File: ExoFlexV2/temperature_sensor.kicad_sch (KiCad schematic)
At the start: 32 parts, among them U31 SN74LVC3G14DCUT_V2, U33 SN74HC7032D_V2, U42 ADCMP602BRMZ, U43 ADCMP602BRMZ, U44 ADCMP602BRMZ, U6 SN74HC7032D_V2, U8 SN74LV4T08PWR_V2

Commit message: quque truc
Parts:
- removed R52, R53, R54: R_Small_US, Resistor_SMD:R_0603_1608Metric, symbol Device:R_Small_US
- removed RV2, RV3, RV4: *, symbol Device:R_Potentiometer_US
- removed TP30, TP31, TP32: 5005, FootPrint:KEYSTONE_5005, symbol SymLib:5005
- added C123, C124, C125, C126, C127, C128: 1nF, Capacitor_SMD:C_0603_1608Metric, symbol Device:C
- added R100, R104, R105, R106, R107, R108, R109, R98, R99: 0 ohm, Resistor_SMD:R_0603_1608Metric, symbol Device:R_Small_US
- added R101, R102, R103, R110, R111, R112: 7,5k, Resistor_SMD:R_0603_1608Metric, symbol Device:R_Small_US
- added TP73, TP74, TP75, TP76, TP77, TP78, TP82: 5005, FootPrint:KEYSTONE_5005, symbol SymLib:5005
- renumbered C98 to C129, C99 to C130, C100 to C131, C101 to C132, C102 to C133, C103 to C134, C104 to C135, C105 to C136, C106 to C137, C107 to C138, C108 to C139, C109 to C140, C110 to C141, TP33 to TP79, TP34 to TP80, TP35 to TP81, U31 to U33, U33 to U35, U42 to U39, U43 to U40, U44 to U41, U6 to U7, U8 to U9
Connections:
- net +5VA: now also R104.1, R106.1, R108.1; no longer C129.2, C130.2, C131.2, C132.2, C133.2, C134.2, C135.2, C136.2, C137.2, C138.2, C139.2, C140.2, C141.2, U39.6 (GND), U40.6 (GND), U41.6 (GND), U7.7 (GND)
- net TEMP_1: now also C124.1, R102.2, TP76.TP
- net TEMP_2: now also C125.1, R103.2, TP77.TP
- net TEMP_3: now also C123.1, R101.2, TP78.TP
- net TEMP_SEC: now also TP82.TP
- net at U39.3 (VN): now also C126.1, R110.2
- net at U41.3 (VN): now also C128.1, R112.2
- net at U40.3 (VN): now also C127.1, R111.2
- new net: R108.2, R109.2, R112.1
- new net: R104.2, R105.2, R110.1
- new net: R99.1, TP74.TP
- new net: R106.2, R107.2, R111.1
- new net: R98.1, TP73.TP
- new net: R100.1, TP75.TP
- new net GND: C123.2, C124.2, C125.2, C126.2, C127.2, C128.2, C129.2, C130.2, C131.2, C132.2, C133.2, C134.2, C135.2, C136.2, C137.2, C138.2, C139.2, C140.2, C141.2, R105.1, R107.1, R109.1, U39.6 (GND), U40.6 (GND), U41.6 (GND), U7.7 (GND)
- new net TEMP_OUT_1: R102.1, R99.2
- new net TEMP_OUT_2: R100.2, R103.1
- new net TEMP_OUT_3: R101.1, R98.2

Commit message: Placement
Début du placement et modification d'après dernier review
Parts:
- removed C123, C125, C127, C128: 1nF, Capacitor_SMD:C_0603_1608Metric, symbol Device:C
- removed C130, C131, C133, C134, C137, C138, C140, C141: 0,01uF, Capacitor_SMD:C_0603_1608Metric, symbol Device:C
- removed C135: 0,1uF, Capacitor_SMD:C_0603_1608Metric, symbol Device:C
- removed R100, R106, R107, R108, R109, R98: 0 ohm, Resistor_SMD:R_0603_1608Metric, symbol Device:R_Small_US
- removed R101, R103, R111, R112: 7,5k, Resistor_SMD:R_0603_1608Metric, symbol Device:R_Small_US
- removed TP73, TP75, TP77, TP78, TP79, TP80, TP81: 5005, FootPrint:KEYSTONE_5005, symbol SymLib:5005
- removed U33: SN74LVC3G14DCUT_V2, FootPrint:SN74LVC3G14DCUT, symbol SymLib:SN74LVC3G14DCUT_V2
- removed U35, U7: SN74HC7032D_V2, FootPrint:SN74HC7032D, symbol SymLib:SN74HC7032D_V2
- removed U40, U41: ADCMP602BRMZ, FootPrint:ADCMP602BRMZ, symbol SymLib:ADCMP602BRMZ
- removed U9: SN74LV4T08PWR_V2, FootPrint:SN74LV4T08PWR, symbol SymLib:SN74LV4T08PWR_V2
- R90: renamed from R99; value 0 ohm -> 0Ω
- renumbered C124 to C127, C126 to C128, C132 to C130, C136 to C131, C139 to C132, R102 to R91, R104 to R92, R105 to R93, R110 to R94, TP74 to TP118, TP76 to TP119, TP82 to TP120, U39 to U38
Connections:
- net TEMP_SEC: now also U38.7 (Q)
- no-connect marks 6 -> 2
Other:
- note removed: "VCCI - U42"
- note removed: "VCCI - U43"
- note removed: "VCCO - U42"
- note removed: "VCCO - U43"
- moved on the sheet: C127, C128, C129, C130, C131, C132, R90, R91, R92, R93, R94, TP118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

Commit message: Placement encore
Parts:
- R93: renamed from R92; value 0 ohm -> 0Ω
- R94: renamed from R93; value 0 ohm -> 0Ω
- renumbered C127 to C128, C128 to C129, C129 to C130, C130 to C131, C131 to C132, C132 to C133, R90 to R91, R91 to R92, R94 to R95
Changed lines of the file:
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@@
   (symbol (lib_id "Device:C") (at 234.95 142.24 0) (unit 1)
     (in_bom yes) (on_board yes)
-    (property "Reference" "C131" (id 0) (at 231.14 139.7 0)
+    (property "Reference" "C132" (id 0) (at 231.14 139.7 0)
       (effects (font (size 1.27 1.27)) (justify left))
     )
@@
   (symbol (lib_id "Device:R_Small_US") (at 113.03 102.87 180) (unit 1)
     (in_bom yes) (on_board yes) (fields_autoplaced)
-    (property "Reference" "R93" (id 0) (at 115.57 101.5999 0)
-      (effects (font (size 1.27 1.27)) (justify right))
-    )
-    (property "Value" "0 ohm" (id 1) (at 115.57 104.1399 0)
+    (property "Reference" "R94" (id 0) (at 115.57 101.5999 0)
+      (effects (font (size 1.27 1.27)) (justify right))
+    )
+    (property "Value" "0Ω" (id 1) (at 115.57 104.1399 0)
       (effects (font (size 1.27 1.27)) (justify right))
     )
@@
   (symbol (lib_id "power:GND") (at 113.03 105.41 0) (unit 1)
     (in_bom yes) (on_board yes) (fields_autoplaced)
-    (property "Reference" "#PWR0203" (id 0) (at 113.03 111.76 0)
+    (property "Reference" "#PWR0204" (id 0) (at 113.03 111.76 0)
       (effects (font (size 1.27 1.27)) hide)
     )
@@
   (symbol (lib_id "power:GND") (at 190.5 99.06 0) (unit 1)
     (in_bom yes) (on_board yes) (fields_autoplaced)
-    (property "Reference" "#PWR0207" (id 0) (at 190.5 105.41 0)
+    (property "Reference" "#PWR0208" (id 0) (at 190.5 105.41 0)
       (effects (font (size 1.27 1.27)) hide)
     )
@@
   (symbol (lib_id "power:+5VA") (at 113.03 86.36 0) (unit 1)
     (in_bom yes) (on_board yes) (fields_autoplaced)
-    (property "Reference" "#PWR0202" (id 0) (at 113.03 90.17 0)
+    (property "Reference" "#PWR0203" (id 0) (at 113.03 90.17 0)
       (effects (font (size 1.27 1.27)) hide)
     )
@@
   (symbol (lib_id "power:+5VA") (at 163.83 77.47 0) (unit 1)
     (in_bom yes) (on_board yes) (fields_autoplaced)
-    (property "Reference" "#PWR0205" (id 0) (at 163.83 81.28 0)
+    (property "Reference" "#PWR0206" (id 0) (at 163.83 81.28 0)
       (effects (font (size 1.27 1.27)) hide)
     )
@@
   (symbol (lib_id "Device:C") (at 245.11 142.24 0) (unit 1)
     (in_bom yes) (on_board yes)
-    (property "Reference" "C132" (id 0) (at 241.3 139.7 0)
+    (property "Reference" "C133" (id 0) (at 241.3 139.7 0)
       (effects (font (size 1.27 1.27)) (justify left))
     )
@@
   (symbol (lib_id "power:GND") (at 245.11 151.13 0) (unit 1)
     (in_bom yes) (on_board yes) (fields_autoplaced)
-    (property "Reference" "#PWR0209" (id 0) (at 245.11 157.48 0)
+    (property "Reference" "#PWR0210" (id 0) (at 245.11 157.48 0)
       (effects (font (size 1.27 1.27)) hide)
     )
@@
   (symbol (lib_id "Device:C") (at 96.52 83.82 0) (unit 1)
     (in_bom yes) (on_board yes) (fields_autoplaced)
-    (property "Reference" "C127" (id 0) (at 100.33 82.5499 0)
+    (property "Reference" "C128" (id 0) (at 100.33 82.5499 0)
       (effects (font (size 1.27 1.27)) (justify left))
     )
@@
   (symbol (lib_id "Device:R_Small_US") (at 113.03 91.44 0) (unit 1)
     (in_bom yes) (on_board yes) (fields_autoplaced)
-    (property "Reference" "R92" (id 0) (at 115.57 90.1699 0)
-      (effects (font (size 1.27 1.27)) (justify left))
-    )
-    (property "Value" "0 ohm" (id 1) (at 115.57 92.7099 0)
+    (property "Reference" "R93" (id 0) (at 115.57 90.1699 0)
+      (effects (font (size 1.27 1.27)) (justify left))
+    )
+    (property "Value" "0Ω" (id 1) (at 115.57 92.7099 0)
       (effects (font (size 1.27 1.27)) (justify left))
     )
@@
   (symbol (lib_id "Device:C") (at 200.66 142.24 0) (unit 1)
     (in_bom yes) (on_board yes)
-    (property "Reference" "C129" (id 0) (at 196.85 139.7 0)
+    (property "Reference" "C130" (id 0) (at 196.85 139.7 0)
       (effects (font (size 1.27 1.27)) (justify left))
     )
@@
   (symbol (lib_id "Device:R_Small_US") (at 72.39 69.85 0) (unit 1)
     (in_bom yes) (on_board yes) (fields_autoplaced)
-    (property "Reference" "R90" (id 0) (at 74.93 68.5799 0)
+    (property "Reference" "R91" (id 0) (at 74.93 68.5799 0)
       (effects (font (size 1.27 1.27)) (justify left))
     )
@@
   (symbol (lib_id "power:+5VA") (at 189.23 77.47 0) (mirror y) (unit 1)
     (in_bom yes) (on_board yes) (fields_autoplaced)
-    (property "Reference" "#PWR0206" (id 0) (at 189.23 81.28 0)
+    (property "Reference" "#PWR0207" (id 0) (at 189.23 81.28 0)
       (effects (font (size 1.27 1.27)) hide)
     )
@@
   (symbol (lib_id "Device:C") (at 210.82 142.24 0) (unit 1)
     (in_bom yes) (on_board yes)
-    (property "Reference" "C130" (id 0) (at 207.01 139.7 0)
+    (property "Reference" "C131" (id 0) (at 207.01 139.7 0)
       (effects (font (size 1.27 1.27)) (justify left))
     )
@@
   (symbol (lib_id "Device:R_Small_US") (at 91.44 77.47 90) (unit 1)
     (in_bom yes) (on_board yes) (fields_autoplaced)
-    (property "Reference" "R91" (id 0) (at 91.44 71.12 90))
+    (property "Reference" "R92" (id 0) (at 91.44 71.12 90))
     (property "Value" "7,5k" (id 1) (at 91.44 73.66 90))
     (property "Footprint" "Resistor_SMD:R_0603_1608Metric" (id 2) (at 91.44 77.47 0)
@@
   (symbol (lib_id "Device:C") (at 143.51 104.14 0) (unit 1)
     (in_bom yes) (on_board yes) (fields_autoplaced)
-    (property "Reference" "C128" (id 0) (at 147.32 102.8699 0)
+    (property "Reference" "C129" (id 0) (at 147.32 102.8699 0)
       (effects (font (size 1.27 1.27)) (justify left))
     )
@@
   (symbol (lib_id "power:GND") (at 96.52 87.63 0) (unit 1)
     (in_bom yes) (on_board yes) (fields_autoplaced)
-    (property "Reference" "#PWR0201" (id 0) (at 96.52 93.98 0)
+    (property "Reference" "#PWR0202" (id 0) (at 96.52 93.98 0)
       (effects (font (size 1.27 1.27)) hide)
     )
@@
   (symbol (lib_id "Device:R_Small_US") (at 138.43 97.79 90) (unit 1)
     (in_bom yes) (on_board yes) (fields_autoplaced)
-    (property "Reference" "R94" (id 0) (at 138.43 91.44 90))
+    (property "Reference" "R95" (id 0) (at 138.43 91.44 90))
     (property "Value" "7,5k" (id 1) (at 138.43 93.98 90))
     (property "Footprint" "Resistor_SMD:R_0603_1608Metric" (id 2) (at 138.43 97.79 0)
@@
   (symbol (lib_id "power:GND") (at 143.51 107.95 0) (unit 1)
     (in_bom yes) (on_board yes) (fields_autoplaced)
-    (property "Reference" "#PWR0204" (id 0) (at 143.51 114.3 0)
+    (property "Reference" "#PWR0205" (id 0) (at 143.51 114.3 0)
       (effects (font (size 1.27 1.27)) hide)
     )
@@
   (symbol (lib_id "power:+5VA") (at 195.58 133.35 0) (unit 1)
     (in_bom yes) (on_board yes)
-    (property "Reference" "#PWR0208" (id 0) (at 195.58 137.16 0)
-      (effects (font (size 1.27 1.27)) hide)
-    )
+    (property "Reference" "#PWR0209" (id 0) (at 195.58 137.16 0)
+      (effects (font (size 1.27 1.27)) hide)
+    )

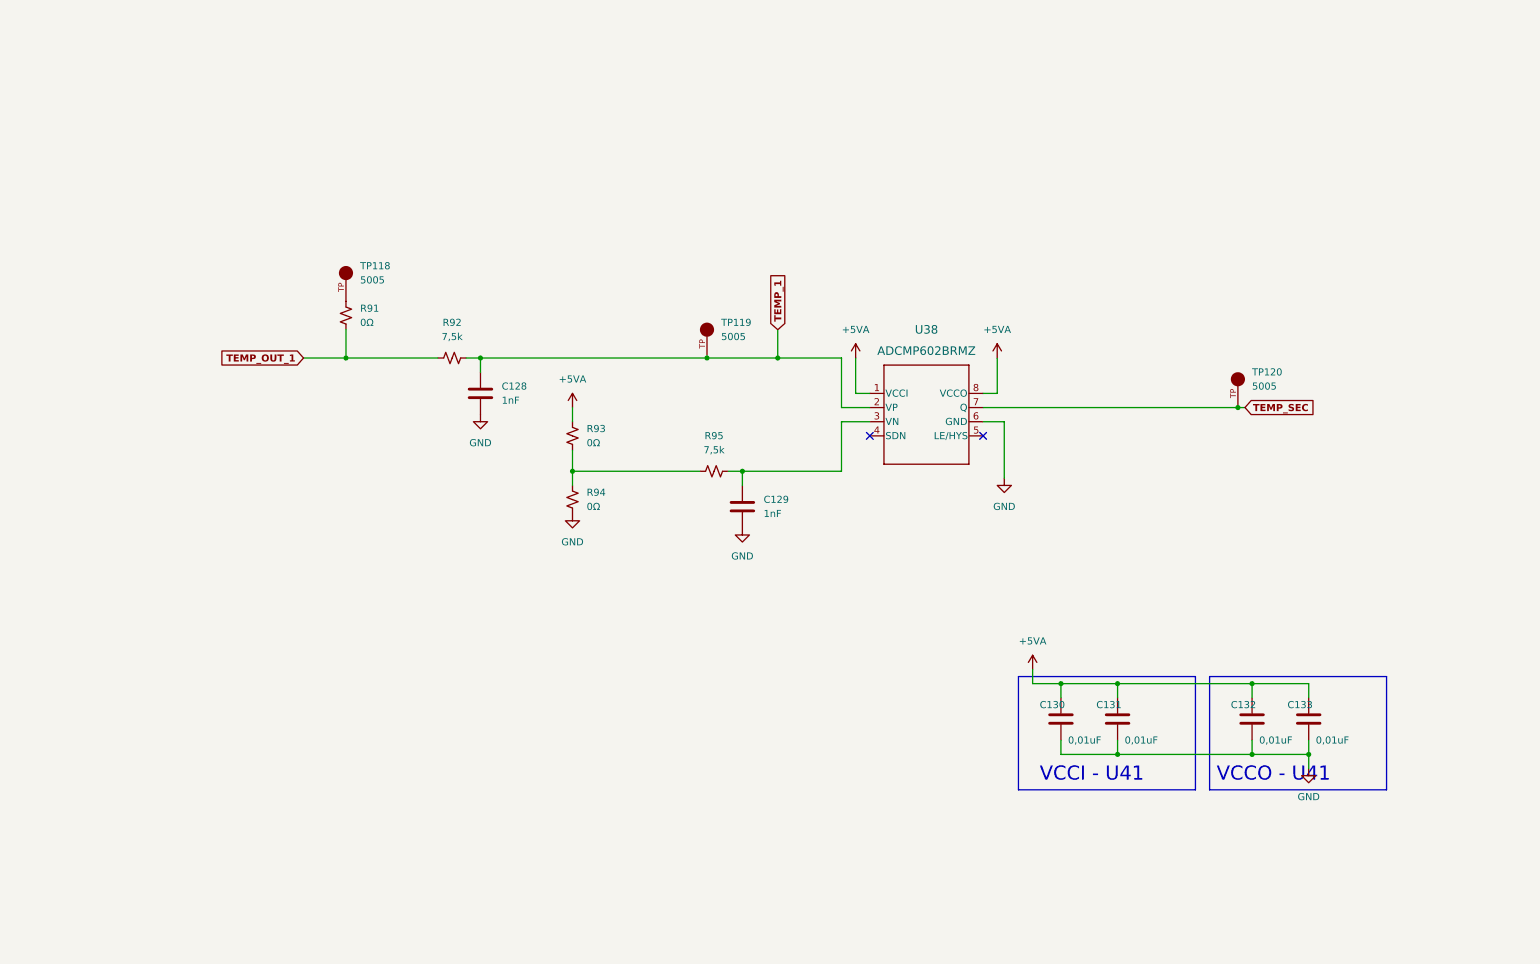
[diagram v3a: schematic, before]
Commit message: Mise à jour mi-stage
- Torque et Amplitude testé et vérifié
- Capteur de présence et de proximité testé
- Système de détection de coupure de fils
- Polyvalence pour plusieurs capteurs
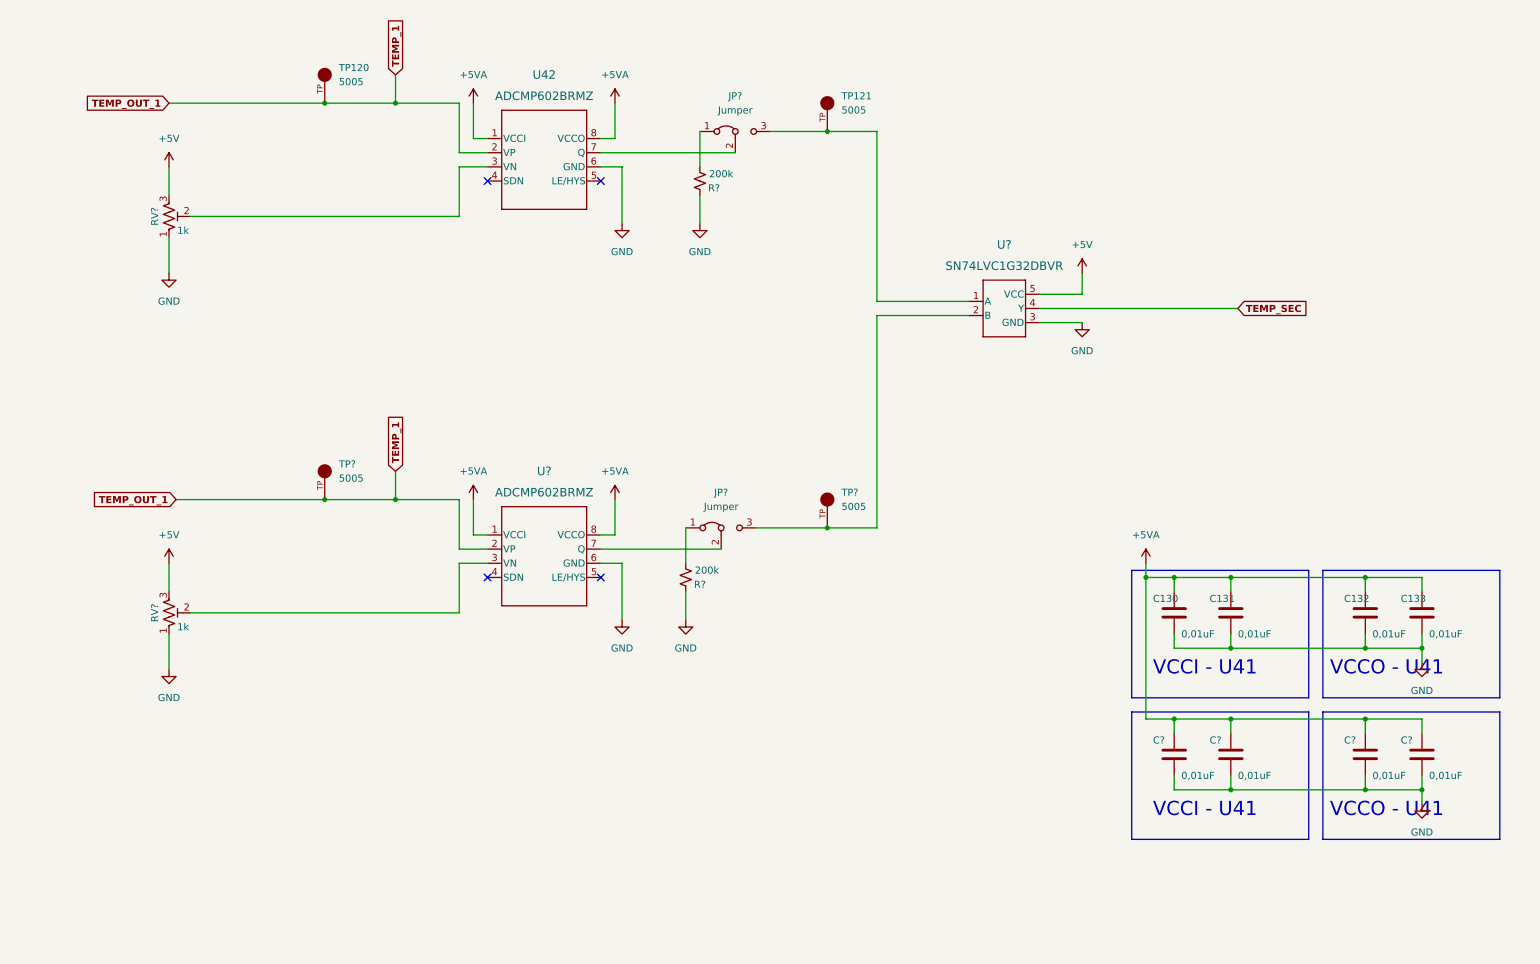
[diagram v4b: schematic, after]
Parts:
- removed C128, C129: 1nF, Capacitor_SMD:C_0603_1608Metric, symbol Device:C
- removed R91, R93, R94: 0Ω, Resistor_SMD:R_0603_1608Metric, symbol Device:R_Small_US
- removed R92, R95: 7,5k, Resistor_SMD:R_0603_1608Metric, symbol Device:R_Small_US
- removed TP118: 5005, FootPrint:KEYSTONE_5005, symbol SymLib:5005
- added C? (x4): 0,01uF, Capacitor_SMD:C_0603_1608Metric, symbol Device:C
- added JP? (x2): Jumper, Connector_PinHeader_2.54mm:PinHeader_1x03_P2.54mm_Vertical, symbol Jumper:Jumper_3_Bridged12
- added R? (x2): 200k, Resistor_SMD:R_0603_1608Metric, symbol Device:R_Small_US
- added RV? (x2): 1k, FootPrint:TRIM_3362P-1-102LF, symbol Device:R_Potentiometer_Trim_US
- added TP? (x2): 5005, FootPrint:KEYSTONE_5005, symbol SymLib:5005
- added U?: ADCMP602BRMZ, FootPrint:ADCMP602BRMZ, symbol SymLib:ADCMP602BRMZ
- added U?: SN74LVC1G32DBVR, FootPrint:SOT95P270X145-5N, symbol SymLib:SN74LVC1G32DBVR
- renumbered TP119 to TP120, TP120 to TP121, U38 to U42
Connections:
- net +5VA: now also C?.1, C?.1, C?.1, C?.1, U?.1 (VCCI), U?.8 (VCCO)
- net GND: now also C?.2, C?.2, C?.2, C?.2, R?.2, R?.2, RV?.1, RV?.1, U?.3 (GND), U?.6 (GND)
- net TEMP_1: now also TP?.TP, U?.2 (VP)
- net TEMP_SEC: now also U?.4 (Y); no longer TP121.TP, U42.7 (Q)
- net at U42.3 (VN): now also RV?.2
- new net: JP?.1 (A), R?.1 (x2)
- new net: JP?.3 (B), TP?.TP, U?.2 (B)
- new net: JP?.2 (C), U42.7 (Q)
- new net: RV?.2, U?.3 (VN)
- new net: JP?.2 (C), U?.7 (Q)
- new net: JP?.3 (B), TP121.TP, U?.1 (A)
- new net +5V: RV?.3, RV?.3, U?.5 (VCC)
- no-connect marks 2 -> 4
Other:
- moved on the sheet: C130, C131, C132, C133, TP120, TP121, U42

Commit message: Mise à jour signaux STM
- Condo de découplage
- Signaux supplémentaire pour le STM
- Page GND sera pour Multiplexeur
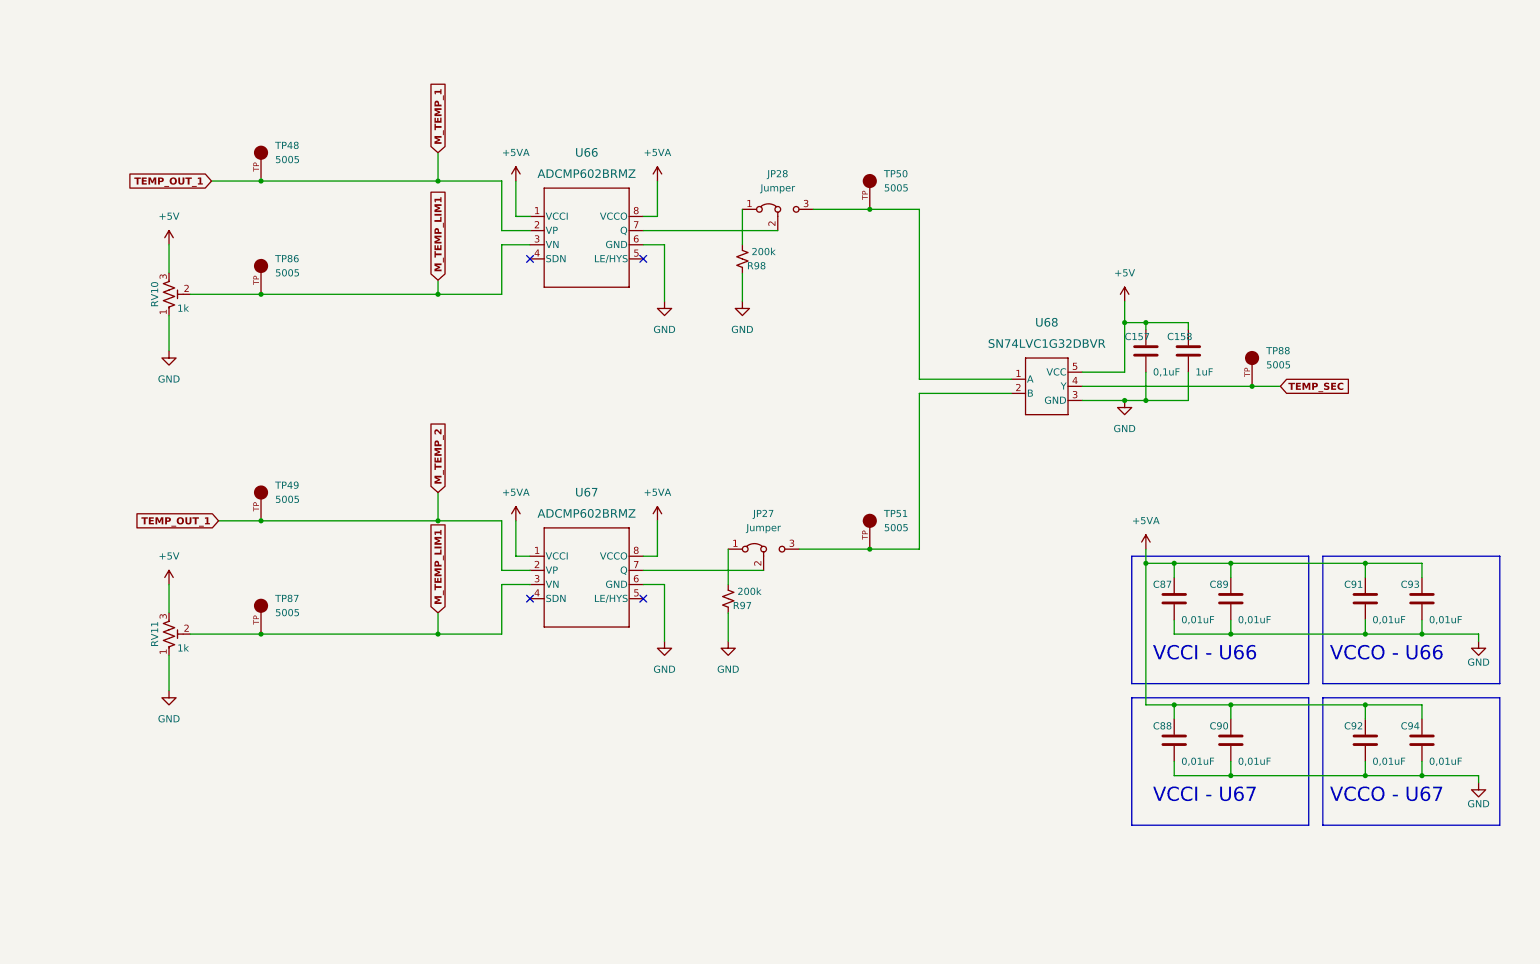
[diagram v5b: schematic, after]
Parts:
- added C157: 0,1uF, Capacitor_SMD:C_0603_1608Metric, symbol Device:C
- added C158: 1uF, Capacitor_SMD:C_0603_1608Metric, symbol Device:C
- added TP86, TP87, TP88: 5005, FootPrint:KEYSTONE_5005, symbol SymLib:5005
- gave numbers to parts that had none: 14
- renumbered C130 to C87, C131 to C89, C132 to C91, C133 to C93, TP120 to TP48, TP121 to TP50, U42 to U66
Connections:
- net +5V: now also C157.1, C158.1
- net GND: now also C157.2, C158.2
- net TEMP_SEC: now also TP88.TP
- net M_TEMP_LIM1: now reaches RV10.2, U66.3 (VN)
- net M_TEMP_LIM1: now also RV11.2, U67.3 (VN), TP86.TP, TP87.TP
- net TEMP_1 renamed M_TEMP_1
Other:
- note added: "VCCI - U66"
- note added: "VCCI - U67"
- note added: "VCCO - U66"
- note added: "VCCO - U67"
- note removed: "VCCI - U41"
- note removed: "VCCO - U41"
- moved on the sheet: C87, C88, C89, C90, C91, C92, C93, C94, JP27, JP28, R97, R98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
